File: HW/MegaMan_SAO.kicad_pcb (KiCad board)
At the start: 2 copper layers, 77.5 x 60 mm, 16 parts, among them X1 Badgelife_sao_connector_v169b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

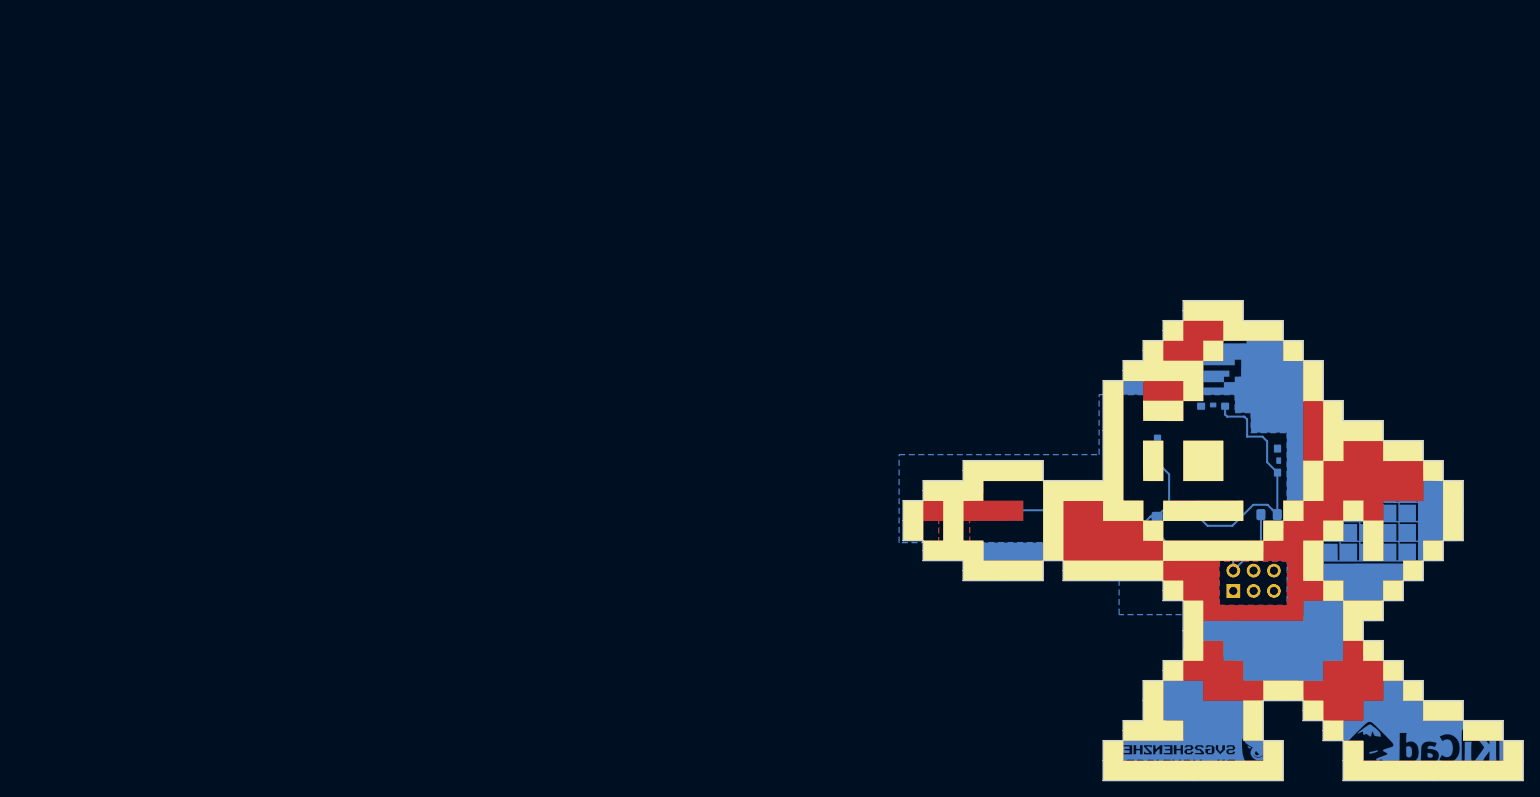
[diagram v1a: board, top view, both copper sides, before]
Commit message: Fixed ground in schematic and made new netlist. Working on layout
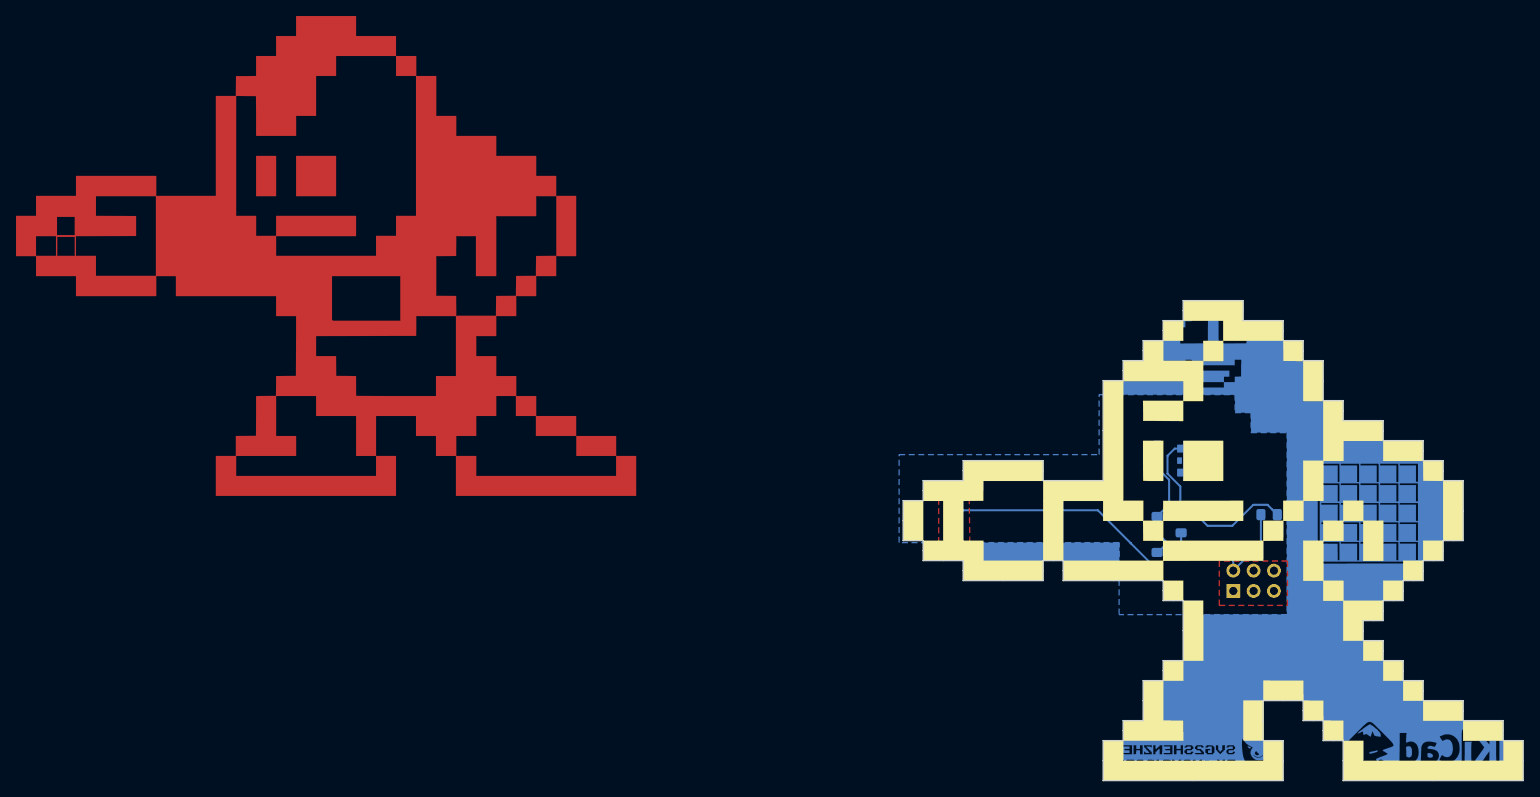
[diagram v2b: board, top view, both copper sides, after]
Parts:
- removed D5: WHT_LED, MegaMan_SAO:1204_SIDE_VIEW_LED
- removed D6: YLW_LED, LED_THT:LED_D5.0mm_Horizontal_O6.35mm_Z3.0mm
- added R4: 100R, Resistor_SMD:R_0805_2012Metric_Pad1.15x1.40mm_HandSolder, B.Cu at (93.0, 102.5)
- D4: value WHT_LED -> YLW_LED; footprint MegaMan_SAO:1204_SIDE_VIEW_LED -> LED_THT:LED_D5.0mm_Horizontal_O6.35mm_Z3.0mm; moved to F.Cu
- G***: value F.Silk -> LOGO
- moved G*** 116.5 mm to (-10.9, 64.4)
- moved D4 27.4 mm to (67.5, 98.8), turned to 90 degrees
- moved D2 12.0 mm to (96.0, 90.0), turned to 90 degrees
- moved D3 9.38 mm to (93.0, 89.5), turned to 270 degrees
- moved R3 4.60 mm to (93.0, 98.0), turned to 90 degrees
- moved R2 3.00 mm to (96.0, 98.0)
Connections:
- D2 pad 2: Net-(D1-Pad2) -> Net-(D2-Pad2)
- D3 pad 2: Net-(D1-Pad2) -> Net-(D3-Pad2)
- R2 pad 2: Net-(D4-Pad2) -> Net-(D2-Pad2)
- R3 pad 2: Net-(D6-Pad2) -> Net-(D3-Pad2)
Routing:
- net Net-(D6-Pad2): track 28.6 -> 0.00 mm
- net Net-(D1-Pad2): track 30.7 -> 12.0 mm
- net Net-(D4-Pad2): track 16.3 -> 28.6 mm
- net Net-(D2-Pad2): track 0.00 -> 10.6 mm
- net Net-(D3-Pad2): track 0.00 -> 7.18 mm
- net VCC: track 22.5 -> 23.8 mm
